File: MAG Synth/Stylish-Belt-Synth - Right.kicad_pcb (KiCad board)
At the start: 2 copper layers, 88.9 x 101.7 mm, 28 parts, among them J1 Amp Board, SW1 Power, U1 stm32f103c8t6-module-china_smd, U2 XPT8871

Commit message: Latest
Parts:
- removed C2: 1uF, Capacitors_ThroughHole:C_Disc_D5.0mm_W2.5mm_P5.00mm
- removed C4: 470uF, Capacitors_SMD:C_0805_HandSoldering
- removed C5: 1uF, Capacitors_SMD:C_0805_HandSoldering
- removed C6: 1uF, Capacitors_ThroughHole:CP_Radial_Tantal_D4.5mm_P2.50mm
- removed C7: 0.39uF, Capacitors_SMD:C_0805_HandSoldering
- removed D0, D1, D2, D4, D5, D6, D7, D8: WS2812B, WS2812B
- removed J2: ~, Pin_Headers:Pin_Header_Straight_1x04_Pitch2.54mm
- removed R4: 10k, Resistors_ThroughHole:R_Axial_DIN0207_L6.3mm_D2.5mm_P2.54mm_Vertical
- removed R5: 1k, Resistors_ThroughHole:R_Axial_DIN0207_L6.3mm_D2.5mm_P2.54mm_Vertical
- removed U1: stm32f103c8t6-module-china_smd, SoftEggKiCAD:stm32f103c8t6-module-china-smd
- added BT1: 4 x 1.5V, Pin_Headers:Pin_Header_Straight_1x02_Pitch2.54mm, B.Cu at (186.1, 57.1)
- added CA1: 470μF, Capacitors_ThroughHole:CP_Radial_Tantal_D4.5mm_P2.50mm, B.Cu at (197.6, 88.9)
- added CA2: 1μF, SoftEggKiCAD:C_Disc_D5.0mm_W2.5mm_P5.00mm+SMD, B.Cu at (197.6, 85.3)
- added CA3: 1μF, SoftEggKiCAD:C_Disc_D5.0mm_W2.5mm_P5.00mm+SMD, B.Cu at (189.9, 92.7)
- added CA4: 0.39μF, SoftEggKiCAD:C_Disc_D5.0mm_W2.5mm_P5.00mm+SMD, B.Cu at (183.4, 84.8)
- added JA1: Conn_01x06, Pin_Headers:Pin_Header_Straight_1x06_Pitch2.54mm, F.Cu at (196.1, 81.8)
- added REF**: AA Battery Holder, SoftEggKiCAD:AA_Battery_Holder_SoftEgg, B.Cu at (215.1, 104.8)
- added REF**: 1pin, Connect:1pin, F.Cu at (222.3, 60.8)
- added REF**: 1pin, Connect:1pin, F.Cu at (222.3, 149.4)
- BT2: footprint Pin_Headers:Pin_Header_Angled_1x02_Pitch2.54mm -> Pin_Headers:Pin_Header_Straight_1x02_Pitch2.54mm
- C1: value 1uF -> 1μF; footprint Capacitors_SMD:C_0805_HandSoldering -> SoftEggKiCAD:C_Disc_D5.0mm_W2.5mm_P5.00mm+SMD
- D3: value WS2812B -> 1N5822; footprint WS2812B -> SoftEggKiCAD:D_DO-35_SOD27_P7.62mm_Horizontal+SMD
- J1: value Amp Board -> Audio-Jack-3_2Switches; footprint Pin_Headers:Pin_Header_Straight_1x06_Pitch2.54mm -> Connectors:Stereo_Jack_3.5mm_Switch_Ledino_KB3SPRS; moved to B.Cu
- KB1: footprint SoftEggKiCAD:MAGWestSynthContactKeybedRight -> SoftEggKiCAD:MAGWestSynthContactKeybed
- LS1: footprint Pin_Headers:Pin_Header_Angled_1x02_Pitch2.54mm -> Pin_Headers:Pin_Header_Straight_1x02_Pitch2.54mm; moved to B.Cu
- R1: value 10k -> 10kΩ; footprint Resistors_SMD:R_0805_HandSoldering -> SoftEggKiCAD:R_Axial_DIN0204_L3.6mm_D1.6mm_P7.62mm_Horizontal+SMD804
- R2: footprint Resistors_SMD:R_0805_HandSoldering -> SoftEggKiCAD:R_Axial_DIN0204_L3.6mm_D1.6mm_P7.62mm_Horizontal+SMD804
- R3: value R -> 100Ω; footprint Resistors_SMD:R_0805_HandSoldering -> SoftEggKiCAD:R_Axial_DIN0204_L3.6mm_D1.6mm_P7.62mm_Horizontal+SMD804
- SW1: footprint Pin_Headers:Pin_Header_Straight_1x03_Pitch2.54mm -> SoftEggKiCAD:MSS22D18+THT
- moved U2 31.6 mm to (195.1, 97.0), turned to 0 degrees
- moved LS1 26.2 mm to (197.6, 61.4), turned to 0 degrees
- moved R3 24.9 mm to (190.0, 88.9), turned to 180 degrees
- moved D3 20.5 mm to (164.5, 57.1), turned to 0 degrees
- moved BT2 15.3 mm to (186.1, 64.1), turned to 180 degrees
- moved SW1 14.0 mm to (178.4, 58.4), turned to 0 degrees
- moved J1 12.9 mm to (213.2, 62.9), turned to 250 degrees
- moved R2 10.8 mm to (179.8, 74.2), turned to 0 degrees
- moved C1 1.78 mm to (190.5, 78.7), turned to 90 degrees
- moved R1 1.19 mm to (187.3, 77.5)
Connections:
- net Net-(KB1-Pad17) renamed /F1
- net Net-(KB1-Pad18) renamed /F#1
- net Net-(KB1-Pad19) renamed /G1
- net Net-(KB1-Pad20) renamed /G#1
- net Net-(KB1-Pad21) renamed /A1
- net Net-(KB1-Pad22) renamed /A#1
- net Net-(KB1-Pad23) renamed /B1
- net Net-(KB1-Pad24) renamed /C2
- BT2 pad 1: /WS2812B-16-LED-RING/GND -> Net-(BT1-Pad2)
- BT2 pad 2: Net-(BT1-Pad1) -> Net-(BT2-Pad2)
- C1 pad 1: /PWM_Audio_Out -> /PWM_OUT
- D3 pad 1: /WS2812B-16-LED-RING/5V -> /+5V
- J1 pad 1: /XH-M125-amp-board/VCC -> /XH-M125-amp-board/OUT+
- J1 pad 2: /WS2812B-16-LED-RING/GND -> /XH-M125-amp-board/OUT+
- J1 pad 3: /WS2812B-16-LED-RING/GND -> /XH-M125-amp-board/OUT-
- J1 pad 4: /PWM_Audio_Out -> Net-(J1-Pad4)
- J1 pad 5: /XH-M125-amp-board/OUT- -> Net-(J1-Pad4)
- LS1 pad 1: /XH-M125-amp-board/OUT+ -> Net-(J1-Pad4)
- R1 pad 2: AUDIO_OUT -> /AUDIO_OUT
- R2 pad 1: /WS2812B-16-LED-RING/GND -> GND
- U2 pad 1: /WS2812B-16-LED-RING/GND -> GND
- U2 pad 3: /WS2812B-16-LED-RING/GND -> GND
- U2 pad 6: /XH-M125-amp-board/VCC -> /+5V
- U2 pad 7: /WS2812B-16-LED-RING/GND -> GND
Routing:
- net /WS2812B-16-LED-RING/5V: track 228.2 -> 0.00 mm, vias 9 -> 0
- net /WS2812B-16-LED-RING/GND: track 202.2 -> 0.00 mm, vias 7 -> 0
- net /+5V: track 0.00 -> 97.7 mm, vias 0 -> 3
- net GND: track 0.00 -> 83.3 mm, vias 0 -> 1
- net AUDIO_OUT: track 62.7 -> 0.00 mm
- net /A#1: track 95.6 -> 39.6 mm
- net /C2: track 111.6 -> 57.7 mm
- net Net-(J1-Pad4): track 0.00 -> 52.6 mm, vias 0 -> 3
- net /F1: track 45.2 -> 0.00 mm, vias 1 -> 0
- net Net-(KB1-Pad16): track 42.0 -> 0.00 mm, vias 1 -> 0
- net /XH-M125-amp-board/OUT+: track 64.0 -> 104.1 mm, vias 0 -> 3
- net Net-(BT1-Pad1): track 48.8 -> 14.7 mm
- net /A1: track 98.4 -> 65.0 mm
- net /XH-M125-amp-board/OUT-: track 54.7 -> 84.7 mm, vias 0 -> 1
- net /G#1: track 87.4 -> 59.2 mm
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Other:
- board size 88.9 x 101.7 mm -> 78.8 x 101.4 mm
- net class Default: trace_width 0.508 -> 0.2
- board text added: "."
- board text added: "MODE"
- board text added: "PATCH"
- board text added: "VALUE"
- board text added: "WRITE"
- board text removed: "20"
- board text removed: "AUDIO"

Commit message: Moving around the gerbers
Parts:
- removed BT1: 4 x 1.5V, Pin_Headers:Pin_Header_Straight_1x02_Pitch2.54mm
- removed BT2: Conn_01x02, Pin_Headers:Pin_Header_Straight_1x02_Pitch2.54mm
- removed C1: 1μF, SoftEggKiCAD:C_Disc_D5.0mm_W2.5mm_P5.00mm+SMD
- removed CA4: 0.39μF, SoftEggKiCAD:C_Disc_D5.0mm_W2.5mm_P5.00mm+SMD
- removed D3: 1N5822, SoftEggKiCAD:D_DO-35_SOD27_P7.62mm_Horizontal+SMD
- removed JA1: Conn_01x06, Pin_Headers:Pin_Header_Straight_1x06_Pitch2.54mm
- removed R1: 10kΩ, SoftEggKiCAD:R_Axial_DIN0204_L3.6mm_D1.6mm_P7.62mm_Horizontal+SMD804
- removed R2: 1k, SoftEggKiCAD:R_Axial_DIN0204_L3.6mm_D1.6mm_P7.62mm_Horizontal+SMD804
- removed R3: 100Ω, SoftEggKiCAD:R_Axial_DIN0204_L3.6mm_D1.6mm_P7.62mm_Horizontal+SMD804
- removed the REF** at (215.1, 104.8)
- removed the REF** at (222.3, 60.8)
- removed the REF** at (222.3, 149.4)
- removed SW1: Power, SoftEggKiCAD:MSS22D18+THT
- added ?: 1pin, Connect:1pin, F.Cu at (222.1, 70.2)
- added BT34: ~, SoftEggKiCAD:AA_Battery_Dual_Terminal, B.Cu at (187.3, 134.0)
- added BTN3: -, SoftEggKiCAD:AA_Battery_-_Terminal, B.Cu at (201.3, 78.1)
- added BTP4: +, SoftEggKiCAD:AA_Battery_+_Terminal, B.Cu at (187.3, 78.1)
- added C2: 1000μF, Capacitors_ThroughHole:CP_Radial_D10.0mm_P5.00mm, B.Cu at (194.2, 66.3)
- added C3: 470μF, Capacitors_ThroughHole:CP_Radial_D10.0mm_P5.00mm, B.Cu at (183.4, 66.3)
- added G***: LOGO, SoftEggKiCAD:SOFTEGG_LOGO2, F.Cu at (196.8, 86.7)
- added REF**: 1pin, Connectors:1pin, F.Cu at (215.9, 82.5)
- added REF**: 1pin, Connectors:1pin, F.Cu at (215.9, 91.4)
- CA1: footprint Capacitors_ThroughHole:CP_Radial_Tantal_D4.5mm_P2.50mm -> SoftEggKiCAD:C_Disc_D5.0mm_W2.5mm_P5.00mm+SMD
- CA3: footprint SoftEggKiCAD:C_Disc_D5.0mm_W2.5mm_P5.00mm+SMD -> Capacitors_ThroughHole:CP_Radial_Tantal_D4.5mm_P2.50mm
- J1: value Audio-Jack-3_2Switches -> Headphone
- KB1: footprint SoftEggKiCAD:MAGWestSynthContactKeybed -> SoftEggKiCAD:MAGWestSynthContactKeybedRight2
- LS1: value SPEAKER -> Speaker
- moved CA1 39.9 mm to (174.0, 56.8), turned to 270 degrees
- moved U2 36.5 mm to (189.2, 61.0), turned to 90 degrees
- moved CA2 35.0 mm to (177.8, 56.5), turned to 270 degrees
- moved CA3 34.0 mm to (181.9, 59.7)
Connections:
- J1 pad 1: /XH-M125-amp-board/OUT+ -> Net-(J1-Pad1)
- J1 pad 2: /XH-M125-amp-board/OUT+ -> Net-(J1-Pad1)
- J1 pad 3: /XH-M125-amp-board/OUT- -> Net-(J1-Pad3)
- LS1 pad 2: /XH-M125-amp-board/OUT- -> Net-(J1-Pad3)
- U2 pad 5: /XH-M125-amp-board/OUT+ -> Net-(J1-Pad3)
- U2 pad 8: /XH-M125-amp-board/OUT- -> Net-(J1-Pad1)
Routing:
- net /LED_DIN: track 0.00 -> 179.2 mm, vias 0 -> 1
- net Net-(BTP4-Pad1): track 0.00 -> 150.4 mm
- net Net-(BTN3-Pad1): track 0.00 -> 127.9 mm
- net GND: track 83.3 -> 196.6 mm, vias 1 -> 0
- net /XH-M125-amp-board/OUT+: track 104.1 -> 0.00 mm, vias 3 -> 0
- net /XH-M125-amp-board/OUT-: track 84.7 -> 0.00 mm, vias 1 -> 0
- net Net-(J1-Pad1): track 0.00 -> 77.0 mm, vias 0 -> 3
- net /+5V: track 97.7 -> 163.6 mm, vias 3 -> 1
- net /F1: track 0.00 -> 39.2 mm, vias 0 -> 1
- net /E1: track 0.00 -> 37.5 mm, vias 0 -> 1
- net /A#1: track 39.6 -> 71.3 mm
- net /C2: track 57.7 -> 89.0 mm
- net Net-(J1-Pad3): track 0.00 -> 31.1 mm
- net Net-(BT2-Pad2): track 26.6 -> 0.00 mm
- net Net-(RA1-Pad1): track 10.0 -> 30.8 mm, vias 0 -> 1
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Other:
- board size 78.8 x 101.4 mm -> 78.8 x 101.6 mm
- net class Default: trace_width 0.2 -> 0.635; via_dia 2.032 -> 1.524
- board text added: "-"
- board text added: "1"
- board text added: "STYLUS"
- board text removed: "+5"
- board text removed: "."
- board text removed: "GND"
- board text removed: "MODE"
- board text removed: "OUT+"
- board text removed: "OUT-"
- board text removed: "PATCH"
- board text removed: "VALUE"
- board text removed: "VCC"
- board text removed: "WRITE"

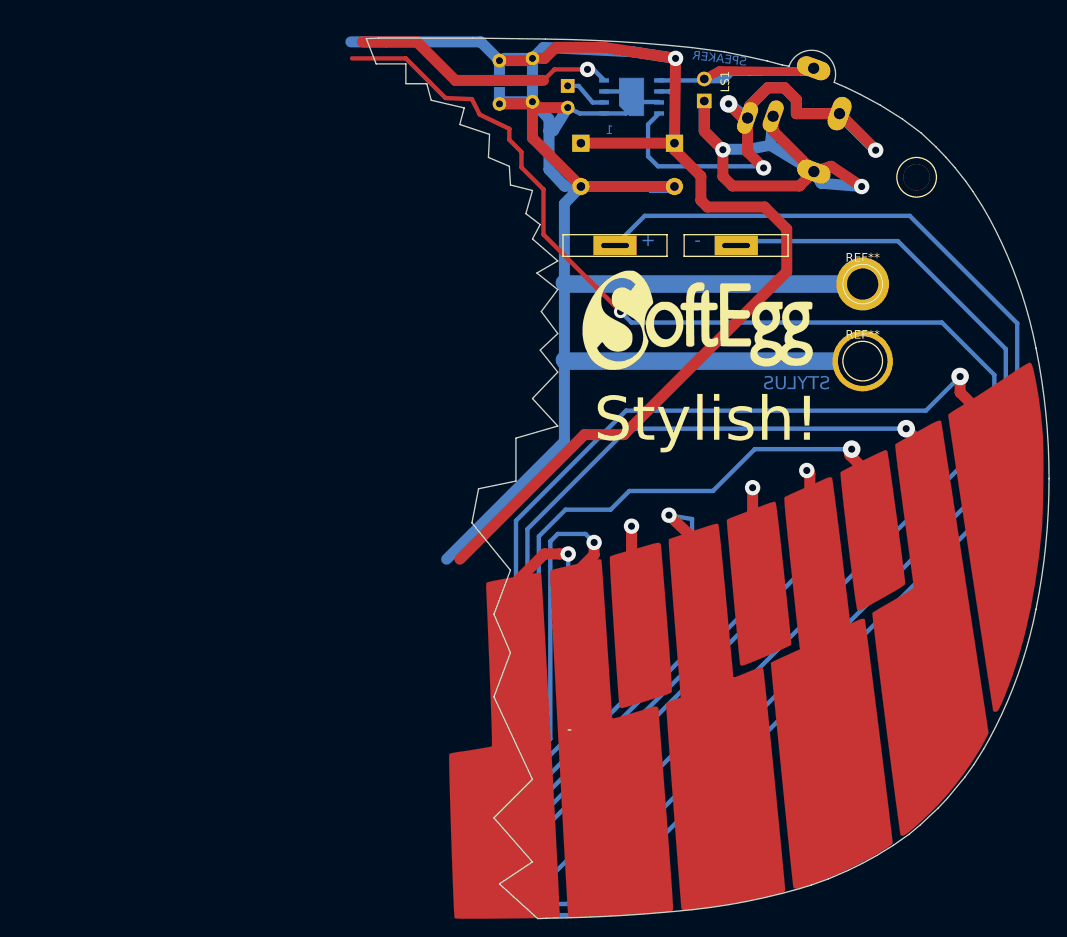
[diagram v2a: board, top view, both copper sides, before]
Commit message: PCB V4 update Wood CNC models added
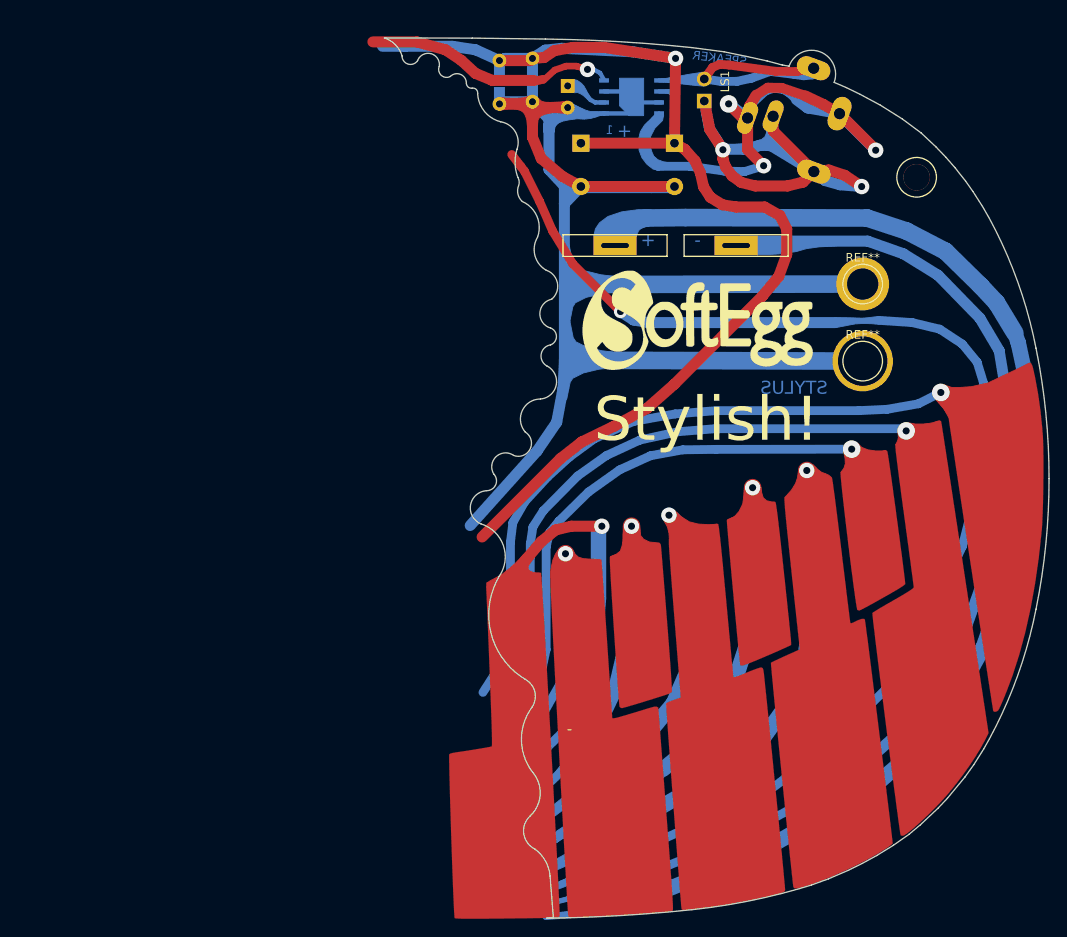
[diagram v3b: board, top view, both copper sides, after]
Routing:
- net /LED_DIN: track 179.2 -> 152.8 mm
- net /F1: track 39.2 -> 27.9 mm
- net /+5V: track 163.6 -> 152.8 mm
- net /E1: track 37.5 -> 46.7 mm
- net /A#1: track 71.3 -> 62.7 mm
- net /C2: track 89.0 -> 80.7 mm
- net /B1: track 77.7 -> 70.0 mm
- net Net-(J1-Pad1): track 77.0 -> 73.8 mm
- net /A1: track 65.4 -> 68.5 mm
- net Net-(J1-Pad4): track 63.5 -> 61.0 mm
- net Net-(BTP4-Pad1): track 150.4 -> 152.4 mm
- net Net-(RA1-Pad1): track 30.8 -> 29.0 mm
- net /F#1: track 48.2 -> 47.1 mm
- net /G#1: track 60.4 -> 61.5 mm
- net Net-(J1-Pad3): track 31.1 -> 32.0 mm
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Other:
- board size 78.8 x 101.6 mm -> 76.7 x 101.6 mm
